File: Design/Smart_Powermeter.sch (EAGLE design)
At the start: 66 parts, among them IC1 AMS1117-3.3, IC3 ESP32-S2-MINI-1-N4R2, J1 AUDIO_JACK_TRRSSMD_RA, J2 AUDIO_JACK_TRRSSMD_RA, J3 AUDIO_JACK_TRRSSMD_RA, J4 AUDIO_JACK_TRRSSMD_RA, J5 AUDIO_JACK_TRRSSMD_RA, J6 AUDIO_JACK_TRRSSMD_RA, J8 USB-C, Q1 IRLML0100

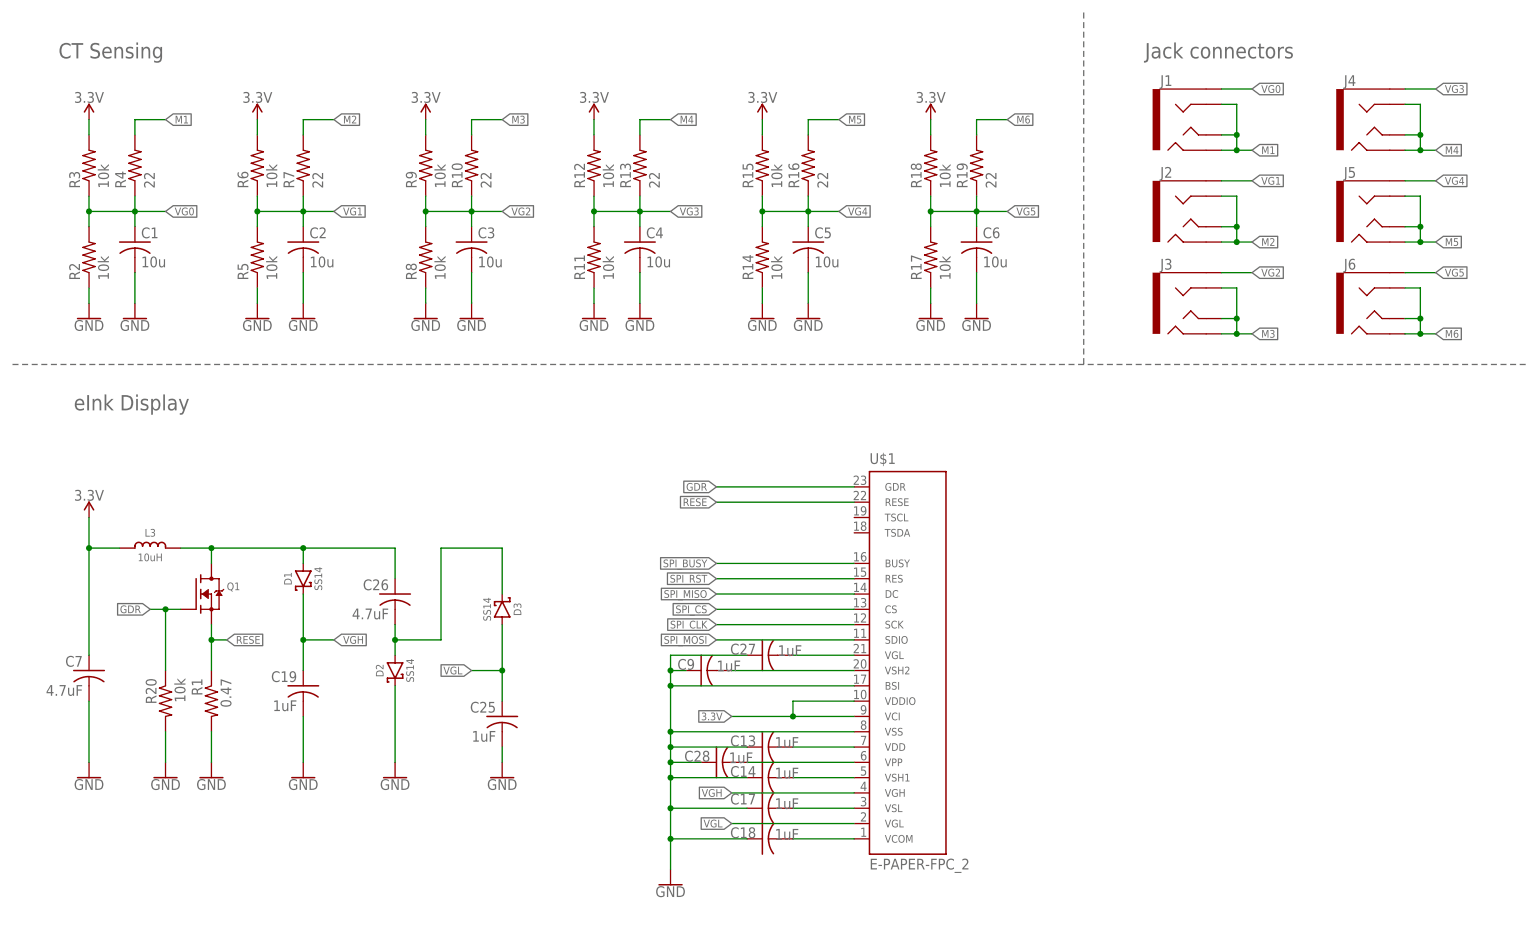
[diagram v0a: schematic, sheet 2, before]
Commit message: Updated design files and silkscreen
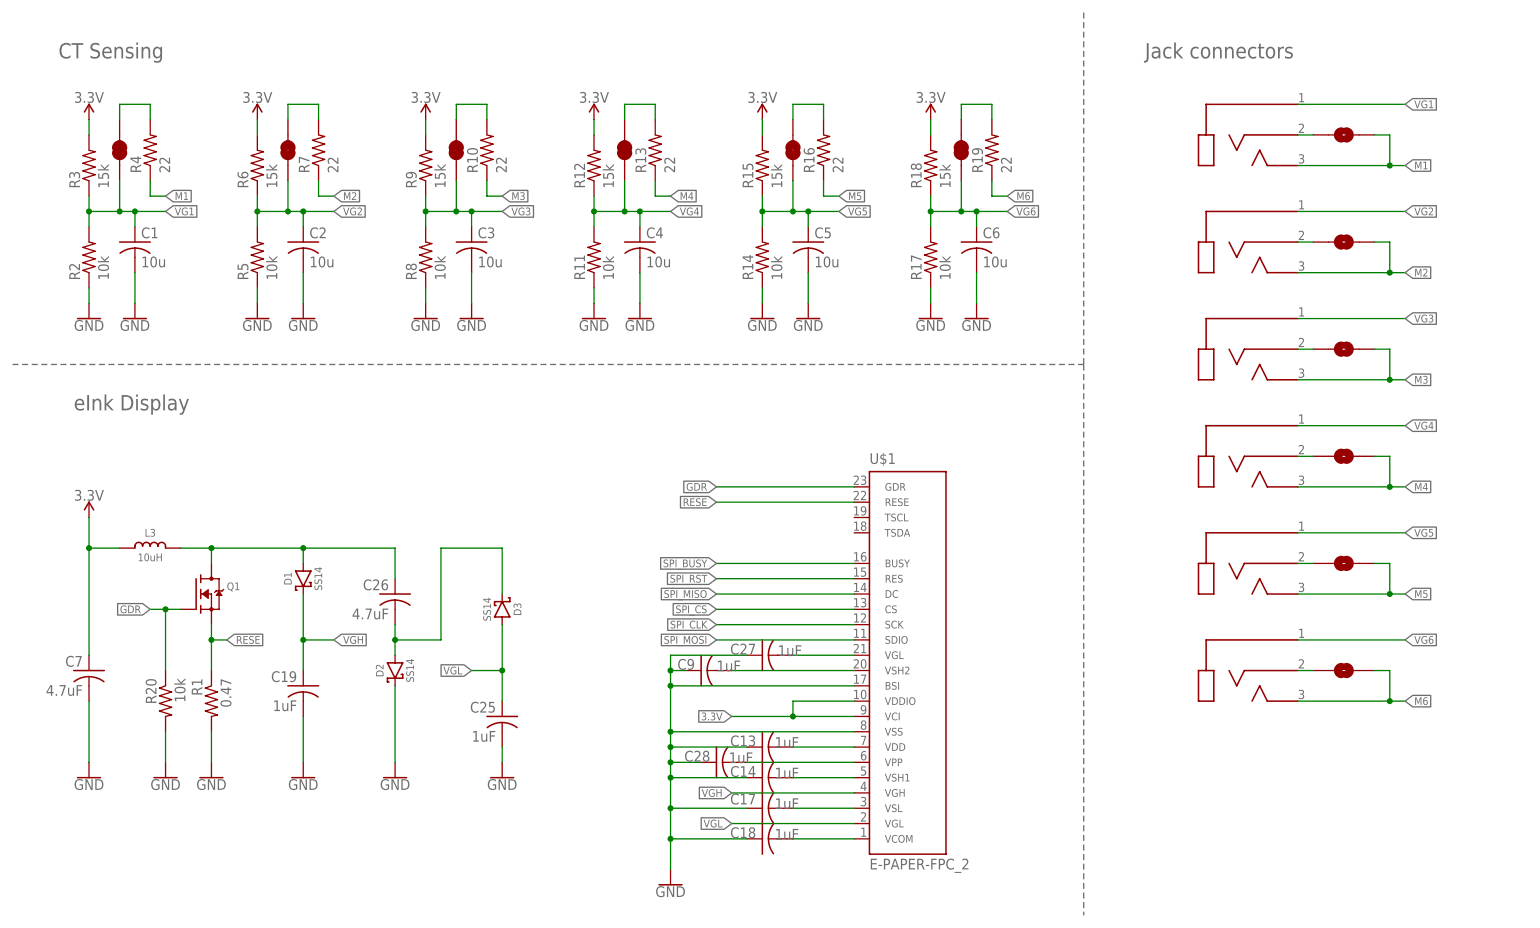
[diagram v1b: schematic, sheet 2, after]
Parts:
- added JP1, JP2, JP3, JP4, JP5, JP6: JUMPER-SMT_2_NC_TRACE_NO-SILK, SparkFun-Jumpers:JUMPER-SMT_2_NC_TRACE_NO-SILK
- added JP10, JP11, JP12, JP7, JP8, JP9: JUMPER-SMT_2_NO_NO-SILK, SparkFun-Jumpers:JUMPER-SMT_2_NO_NO-SILK
- added JP13: JUMPER-SMT_2_NC_PASTE_NO-SILK, SparkFun-Jumpers:JUMPER-SMT_2_NC_PASTE_NO-SILK
- added LED1: GREEN, SparkFun-LED:LED-GREEN0603
- added LED2: BLUE, SparkFun-LED:LED-BLUE0603
- added R21: 330, rcl:R-US_R0603
- added R22: 470, rcl:R-US_R0603
- J1, J2, J3, J4, J5, J6: value AUDIO_JACK_TRRSSMD_RA -> AUDIO_JACK_MONO_3.5_3P; device SparkFun-Connectors:AUDIO_JACK_TRRSSMD_RA -> SpaceDIY_connectors:AUDIO_JACK_MONO_3.5_3P
- R10, R13, R16, R19, R4, R7: device rcl:R-US_R1206 -> rcl:R-US_R0603
- R12, R15, R18, R3, R6, R9: value 10k -> 15k
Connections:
- removed net VG0: C1.1, J1.EARTH, R2.2, R3.1, R4.1
- new net LED: IC3.IO8, R21.2
- new net N$10: J2.2, JP8.2
- new net N$18: J3.2, JP9.2
- new net N$19: J4.2, JP10.2
- new net N$20: J5.2, JP11.2
- new net N$21: J6.2, JP12.2
- new net N$22: JP13.2, R22.2
- new net N$29: LED2.A, R21.1
- new net N$3: JP1.2, R4.2
- new net N$33: LED1.A, R22.1
- new net N$4: JP2.2, R7.2
- new net N$5: JP3.2, R10.2
- new net N$6: JP4.2, R13.2
- new net N$7: JP5.2, R16.2
- new net N$8: JP6.2, R19.2
- new net N$9: J1.2, JP7.2
- new net VG6: C6.1, J6.1, JP6.1, R17.2, R18.1
- net 3.3V: now also JP13.1
- net GND: now also LED1.C, LED2.C
- net M1: now also J1.3, JP7.1, R4.1; no longer J1.RING1, J1.RING2, J1.TIP, R4.2
- net M2: now also J2.3, JP8.1, R7.1; no longer J2.RING1, J2.RING2, J2.TIP, R7.2
- net M3: now also J3.3, JP9.1, R10.1; no longer J3.RING1, J3.RING2, J3.TIP, R10.2
- net M4: now also J4.3, JP10.1, R13.1; no longer J4.RING1, J4.RING2, J4.TIP, R13.2
- net M5: now also J5.3, JP11.1, R16.1; no longer J5.RING1, J5.RING2, J5.TIP, R16.2
- net M6: now also J6.3, JP12.1, R19.1; no longer J6.RING1, J6.RING2, J6.TIP, R19.2
- net VG1: now also C1.1, J1.1, JP1.1, R2.2, R3.1; no longer C2.1, J2.EARTH, R5.2, R6.1, R7.1
- net VG2: now also C2.1, J2.1, JP2.1, R5.2, R6.1; no longer C3.1, J3.EARTH, R10.1, R8.2, R9.1
- net VG3: now also C3.1, J3.1, JP3.1, R8.2, R9.1; no longer C4.1, J4.EARTH, R11.2, R12.1, R13.1
- net VG4: now also C4.1, J4.1, JP4.1, R11.2, R12.1; no longer C5.1, J5.EARTH, R14.2, R15.1, R16.1
- net VG5: now also C5.1, J5.1, JP5.1, R14.2, R15.1; no longer C6.1, J6.EARTH, R17.2, R18.1, R19.1
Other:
- note added: "LED indicators"
- moved on the sheet: R10, R13, R16, R19, R4, R7, U$2, X1-1, X1-2
